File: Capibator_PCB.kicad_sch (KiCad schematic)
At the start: 0 parts

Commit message: Schematic Completed
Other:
- removed sheet Battery_Backup
- removed sheet Heater
- removed sheet RTC
- removed sheet Sensors
- removed sheet Turner
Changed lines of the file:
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@@
     (company "capistor.com")
   )
-  (sheet (at 104.14 129.54) (size 29.21 17.78) (fields_autoplaced)
+  (sheet (at 123.825 114.3) (size 27.94 17.78)
     (stroke (width 0.1524) (type solid))
     (fill (color 0 0 0 0.0000))
-    (property "Sheetname" "Heater" (at 104.14 128.8284 0)
-      (effects (font (size 1.27 1.27)) (justify left bottom))
+    (property "Sheetname" "Outputs " (at 123.19 125.095 0)
+      (effects (font (size 5 5)) (justify left bottom))
     )
-    (property "Sheetfile" "heater.kicad_sch" (at 104.14 147.9046 0)
+    (property "Sheetfile" "outputs.kicad_sch" (at 123.825 132.6646 0)
       (effects (font (size 1.27 1.27)) (justify left top))
     )
     (instances
       (project "Capibator_PCB"
-        (path "/314af396-fc31-4fe3-9f85-bbd0c4bf0b50" (page "7"))
+        (path "/314af396-fc31-4fe3-9f85-bbd0c4bf0b50" (page "4"))
       )
     )
   )
-  (sheet (at 33.02 100.33) (size 27.94 17.78) (fields_autoplaced)
+  (sheet (at 123.825 60.325) (size 30.48 15.24)
     (stroke (width 0.1524) (type solid))
     (fill (color 0 0 0 0.0000))
-    (property "Sheetname" "Outputs " (at 33.02 99.6184 0)
-      (effects (font (size 1.27 1.27)) (justify left bottom))
+    (property "Sheetname" "MCU" (at 129.54 70.485 0)
+      (effects (font (size 5 5)) (justify left bottom))
     )
-    (property "Sheetfile" "outputs.kicad_sch" (at 33.02 118.6946 0)
-      (effects (font (size 1.27 1.27)) (justify left top))
-    )
-    (instances
-      (project "Capibator_PCB"
-        (path "/314af396-fc31-4fe3-9f85-bbd0c4bf0b50" (page "8"))
-      )
-    )
-  )
-  (sheet (at 33.02 73.66) (size 27.94 16.51) (fields_autoplaced)
-    (stroke (width 0.1524) (type solid))
-    (fill (color 0 0 0 0.0000))
-    (property "Sheetname" "Battery_Backup" (at 33.02 72.9484 0)
-      (effects (font (size 1.27 1.27)) (justify left bottom))
-    )
-    (property "Sheetfile" "Battery_Backup.kicad_sch" (at 33.02 90.7546 0)
-      (effects (font (size 1.27 1.27)) (justify left top))
-    )
-    (instances
-      (project "Capibator_PCB"
-        (path "/314af396-fc31-4fe3-9f85-bbd0c4bf0b50" (page "9"))
-      )
-    )
-  )
-  (sheet (at 66.04 73.66) (size 30.48 15.24) (fields_autoplaced)
-    (stroke (width 0.1524) (type solid))
-    (fill (color 0 0 0 0.0000))
-    (property "Sheetname" "MCU" (at 66.04 72.9484 0)
-      (effects (font (size 1.27 1.27)) (justify left bottom))
-    )
-    (property "Sheetfile" "MCU.kicad_sch" (at 66.04 89.4846 0)
+    (property "Sheetfile" "MCU.kicad_sch" (at 123.825 76.1496 0)
       (effects (font (size 1.27 1.27)) (justify left top))
     )
@@
     )
   )
-  (sheet (at 104.14 73.66) (size 29.21 15.24) (fields_autoplaced)
+  (sheet (at 123.19 86.36) (size 29.21 15.24)
     (stroke (width 0.1524) (type solid))
     (fill (color 0 0 0 0.0000))
-    (property "Sheetname" "Power" (at 104.14 72.9484 0)
-      (effects (font (size 1.27 1.27)) (justify left bottom))
+    (property "Sheetname" "Power" (at 126.365 95.885 0)
+      (effects (font (size 5 5)) (justify left bottom))
     )
-    (property "Sheetfile" "power.kicad_sch" (at 104.14 89.4846 0)
+    (property "Sheetfile" "power.kicad_sch" (at 123.19 102.1846 0)
       (effects (font (size 1.27 1.27)) (justify left top))
     )
@@
       )
     )
-  )
-  (sheet (at 66.04 100.33) (size 30.48 17.78) (fields_autoplaced)
-    (stroke (width 0.1524) (type solid))
-    (fill (color 0 0 0 0.0000))
-    (property "Sheetname" "Sensors" (at 66.04 99.6184 0)
-      (effects (font (size 1.27 1.27)) (justify left bottom))
-    )
-    (property "Sheetfile" "untitled.kicad_sch" (at 66.04 118.6946 0)
-      (effects (font (size 1.27 1.27)) (justify left top))
-    )
-    (instances
-      (project "Capibator_PCB"
-        (path "/314af396-fc31-4fe3-9f85-bbd0c4bf0b50" (page "4"))
-      )
-    )
-  )
-  (sheet (at 66.04 129.54) (size 30.48 17.78) (fields_autoplaced)
-    (stroke (width 0.1524) (type solid))
-    (fill (color 0 0 0 0.0000))
-    (property "Sheetname" "Turner" (at 66.04 128.8284 0)
-      (effects (font (size 1.27 1.27)) (justify left bottom))
-    )
-    (property "Sheetfile" "turner.kicad_sch" (at 66.04 147.9046 0)
-      (effects (font (size 1.27 1.27)) (justify left top))
-    )
-    (instances
-      (project "Capibator_PCB"
-        (path "/314af396-fc31-4fe3-9f85-bbd0c4bf0b50" (page "6"))
-      )
-    )
-  )
-  (sheet (at 104.14 100.33) (size 29.21 17.78) (fields_autoplaced)
-    (stroke (width 0.1524) (type solid))
-    (fill (color 0 0 0 0.0000))
-    (property "Sheetname" "RTC" (at 104.14 99.6184 0)
-      (effects (font (size 1.27 1.27)) (justify left bottom))
-    )
-    (property "Sheetfile" "rtc.kicad_sch" (at 104.14 118.6946 0)
-      (effects (font (size 1.27 1.27)) (justify left top))
-    )
-    (instances
-      (project "Capibator_PCB"
-        (path "/314af396-fc31-4fe3-9f85-bbd0c4bf0b50" (page "5"))
-      )
-    )

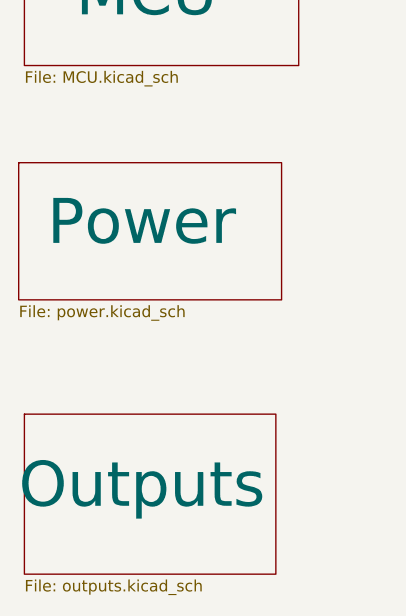
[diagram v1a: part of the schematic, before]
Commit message: assigned footprints. another look needed. moving to pcb
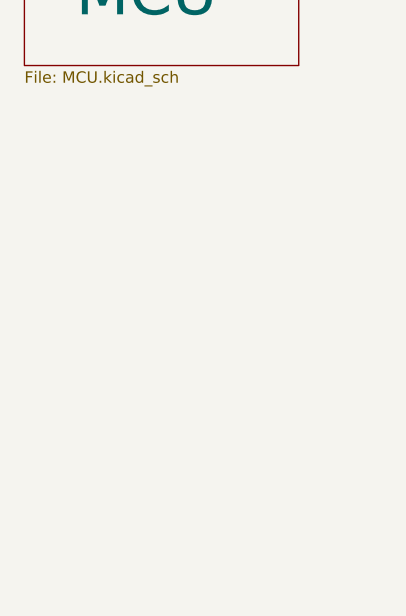
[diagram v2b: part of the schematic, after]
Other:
- removed sheet Outputs 
- removed sheet Power
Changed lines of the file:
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@@
     (company "capistor.com")
-  )
-  (sheet (at 123.825 114.3) (size 27.94 17.78)
-    (stroke (width 0.1524) (type solid))
-    (fill (color 0 0 0 0.0000))
-    (property "Sheetname" "Outputs " (at 123.19 125.095 0)
-      (effects (font (size 5 5)) (justify left bottom))
-    )
-    (property "Sheetfile" "outputs.kicad_sch" (at 123.825 132.6646 0)
-      (effects (font (size 1.27 1.27)) (justify left top))
-    )
-    (instances
-      (project "Capibator_PCB"
-        (path "/314af396-fc31-4fe3-9f85-bbd0c4bf0b50" (page "4"))
-      )
-    )
   )
   (sheet (at 123.825 60.325) (size 30.48 15.24)
@@
       )
     )
-  )
-  (sheet (at 123.19 86.36) (size 29.21 15.24)
-    (stroke (width 0.1524) (type solid))
-    (fill (color 0 0 0 0.0000))
-    (property "Sheetname" "Power" (at 126.365 95.885 0)
-      (effects (font (size 5 5)) (justify left bottom))
-    )
-    (property "Sheetfile" "power.kicad_sch" (at 123.19 102.1846 0)
-      (effects (font (size 1.27 1.27)) (justify left top))
-    )
-    (instances
-      (project "Capibator_PCB"
-        (path "/314af396-fc31-4fe3-9f85-bbd0c4bf0b50" (page "3"))
-      )
-    )
